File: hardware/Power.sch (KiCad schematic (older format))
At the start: 30 parts, among them J8 Batt, Q10 AO3401A, Q11 AO3400 (A09T), Q12 AO3401A, Q13 AO3400 (A09T), Q14 AO3400 (A09T), Q9 AO3400 (A09T), U1 TP4056, U3 DW-01, U8 HX9193-33GB

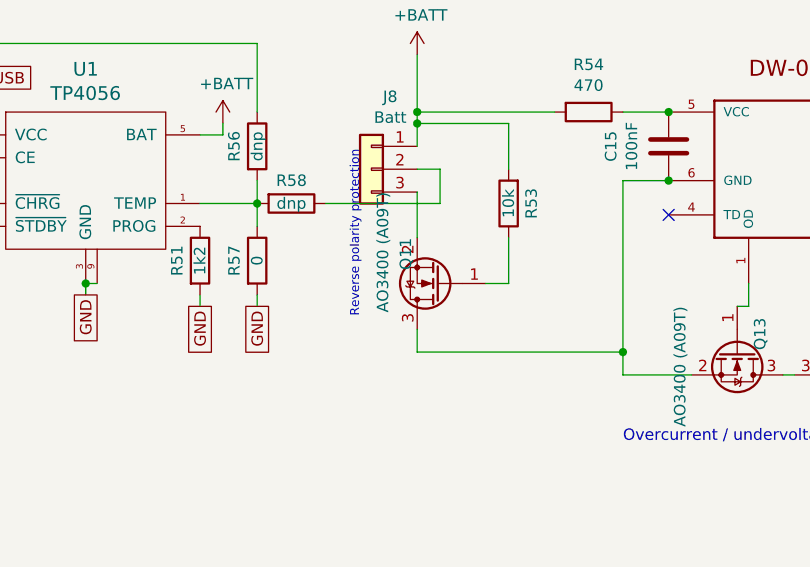
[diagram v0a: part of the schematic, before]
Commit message: Revert "Fixed polarity battery protection"
This reverts commit d596a3d4647cf381d02caddfcfeb8f064578e0bb.
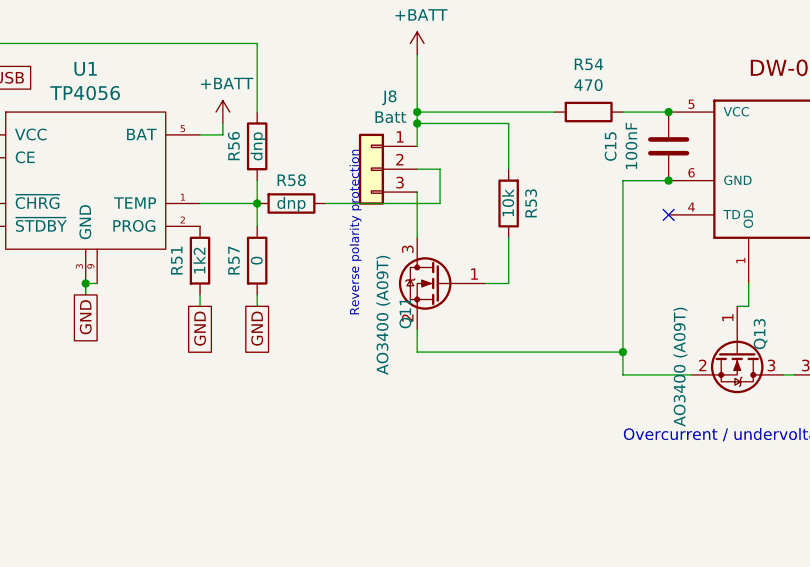
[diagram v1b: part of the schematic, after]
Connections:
- net at C15.2, Q13.2 (S), U3.6 (GND): now also Q11.2 (S); no longer Q11.3 (D)
- net at J8.3 (Pin_3): now also Q11.3 (D); no longer Q11.2 (S)
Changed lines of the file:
@@
 F 4 "C20917" H 5150 4550 50  0001 C CNN "LCSC"
 	1    5150 4550
-	-1   0    0    1
+	-1   0    0    -1
 $EndComp
 $Comp

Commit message: Fixed polarity battery protection
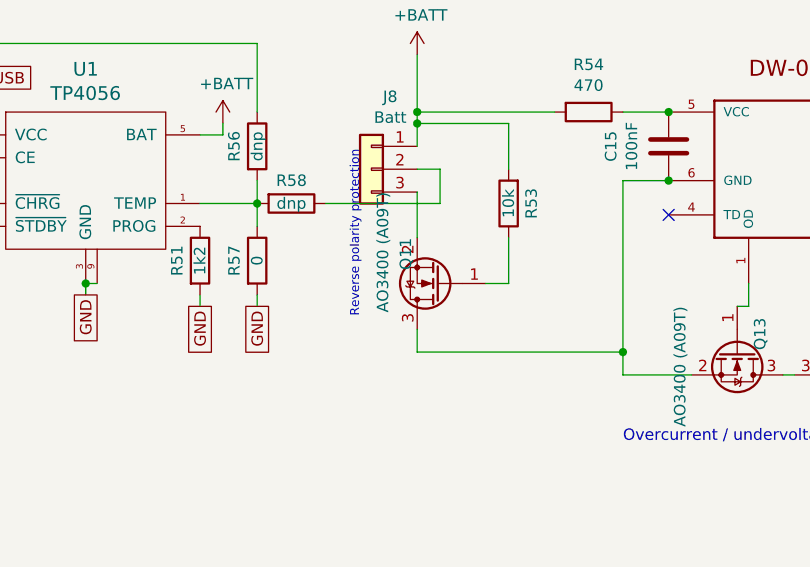
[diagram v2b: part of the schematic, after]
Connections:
- net at C15.2, Q13.2 (S), U3.6 (GND): now also Q11.3 (D); no longer Q11.2 (S)
- net at J8.3 (Pin_3): now also Q11.2 (S); no longer Q11.3 (D)
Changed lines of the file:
@@
 F 4 "C20917" H 5150 4550 50  0001 C CNN "LCSC"
 	1    5150 4550
-	-1   0    0    -1
+	-1   0    0    1
 $EndComp
 $Comp
